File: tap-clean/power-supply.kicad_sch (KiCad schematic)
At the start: 12 parts, among them Q1 TIP42, U2 LM7805_TO220

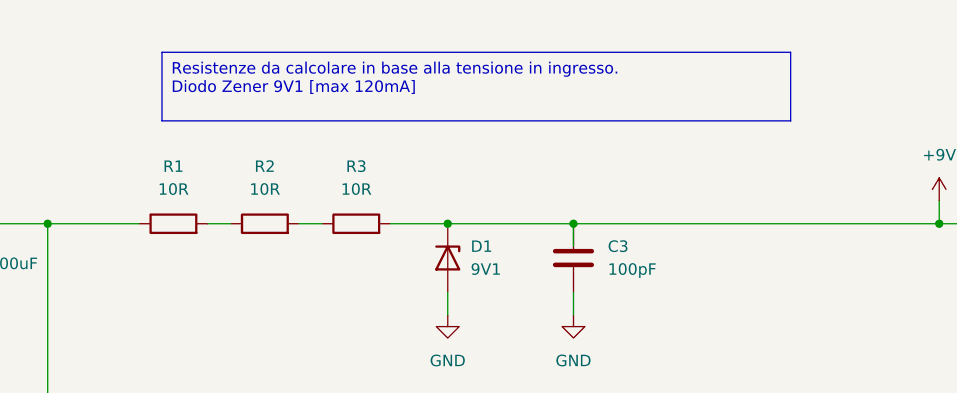
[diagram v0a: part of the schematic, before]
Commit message: adding footprint to connections
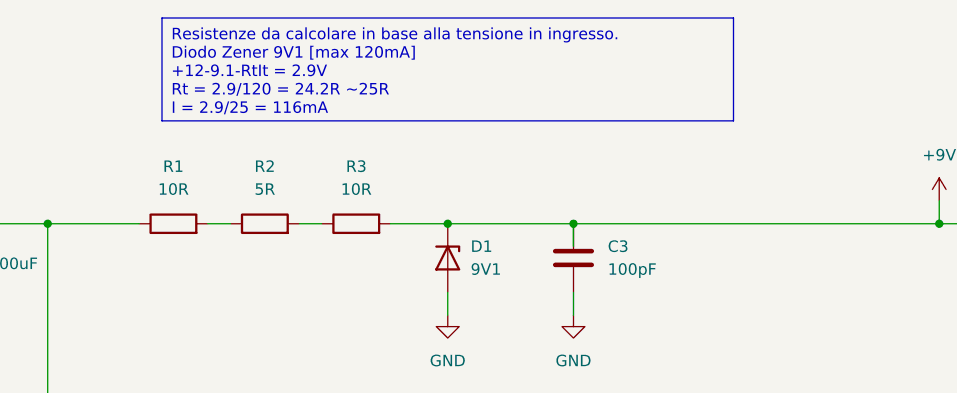
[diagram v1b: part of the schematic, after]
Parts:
- R2: value 10R -> 5R
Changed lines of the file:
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@@
     (stroke (width 0) (type default))
   )
-  (text_box "Resistenze da calcolare in base alla tensione in ingresso.\nDiodo Zener 9V1 [max 120mA]"
-    (at 106.68 17.78 0) (size 69.85 7.62)
+  (text_box "Resistenze da calcolare in base alla tensione in ingresso.\nDiodo Zener 9V1 [max 120mA]\n+12-9.1-RtIt = 2.9V\nRt = 2.9/120 = 24.2R ~25R\nI = 2.9/25 = 116mA"
+    (at 106.68 13.97 0) (size 63.5 11.43)
     (stroke (width 0) (type default))
     (fill (type none))
@@
       (effects (font (size 1.27 1.27)))
     )
-    (property "Value" "10R" (at 118.11 33.02 90)
-      (effects (font (size 1.27 1.27)))
-    )
+    (property "Value" "5R" (at 118.11 33.02 90)
+      (effects (font (size 1.27 1.27)))
+    )
